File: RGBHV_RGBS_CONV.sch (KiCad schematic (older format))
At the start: 38 parts, among them J1 DIGITAL RGB, J10 AUDIO1, J11 RGBHV_2, J12 AUDIO2, J15 RGBS_OUT1, J16 RGBS_OUT2, J17 VIN, J2 VGA DB15, J3 ANALOG RGB DA15, J4 X1, J5 DIGITAL_RGBHV_1, J6 ANALOG RGB, J7 DIGITAL_RGBHV_2, J8 SWITCHER, J9 RGBHV_1, U1 OUT_GND_IN_3.3V, U2 74HC86, U3 OUT_IN_GND_3.3V

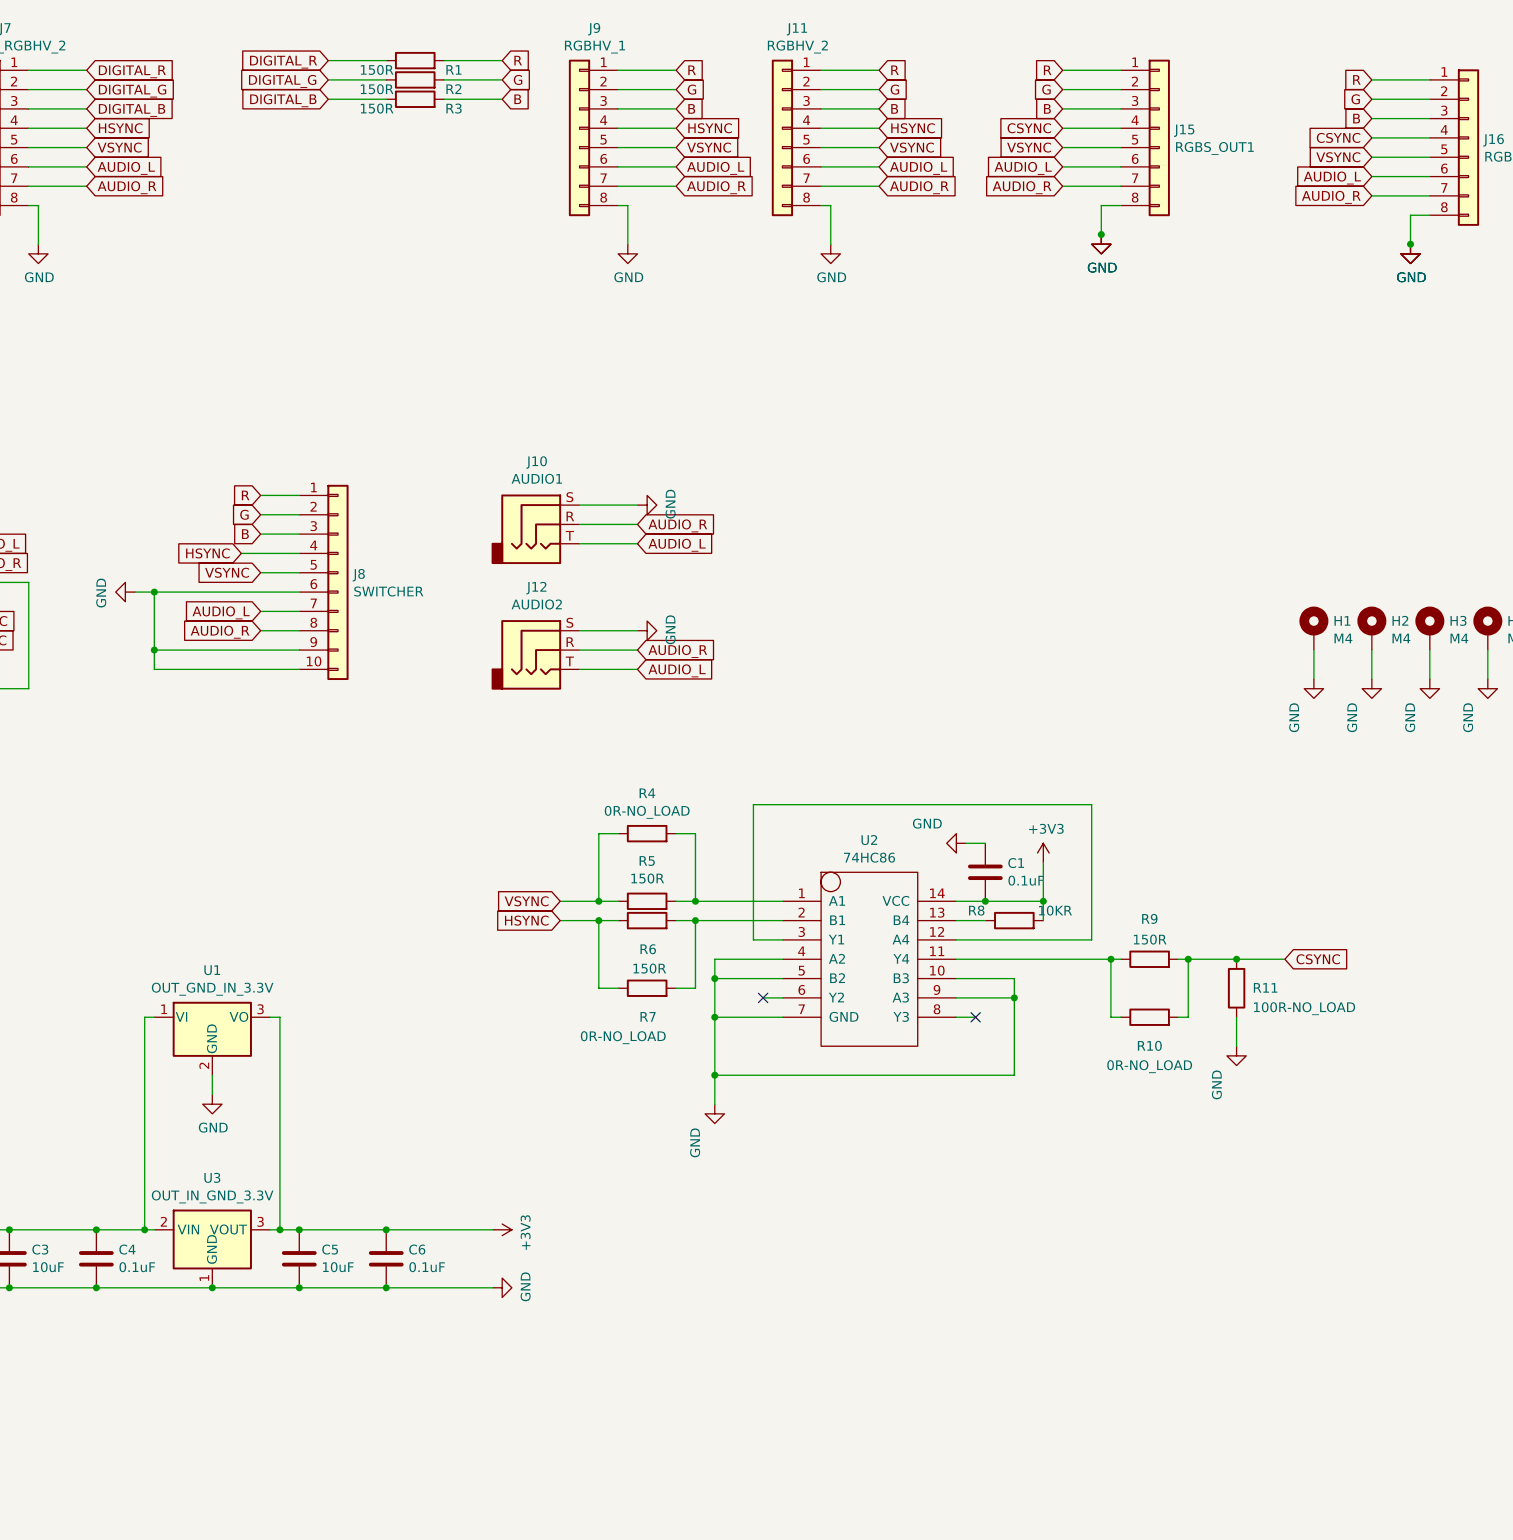
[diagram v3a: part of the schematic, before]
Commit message: Rev1.0C
レギュレータのパターンを追加。
RGBS XHコネクタへの音声パターンカット
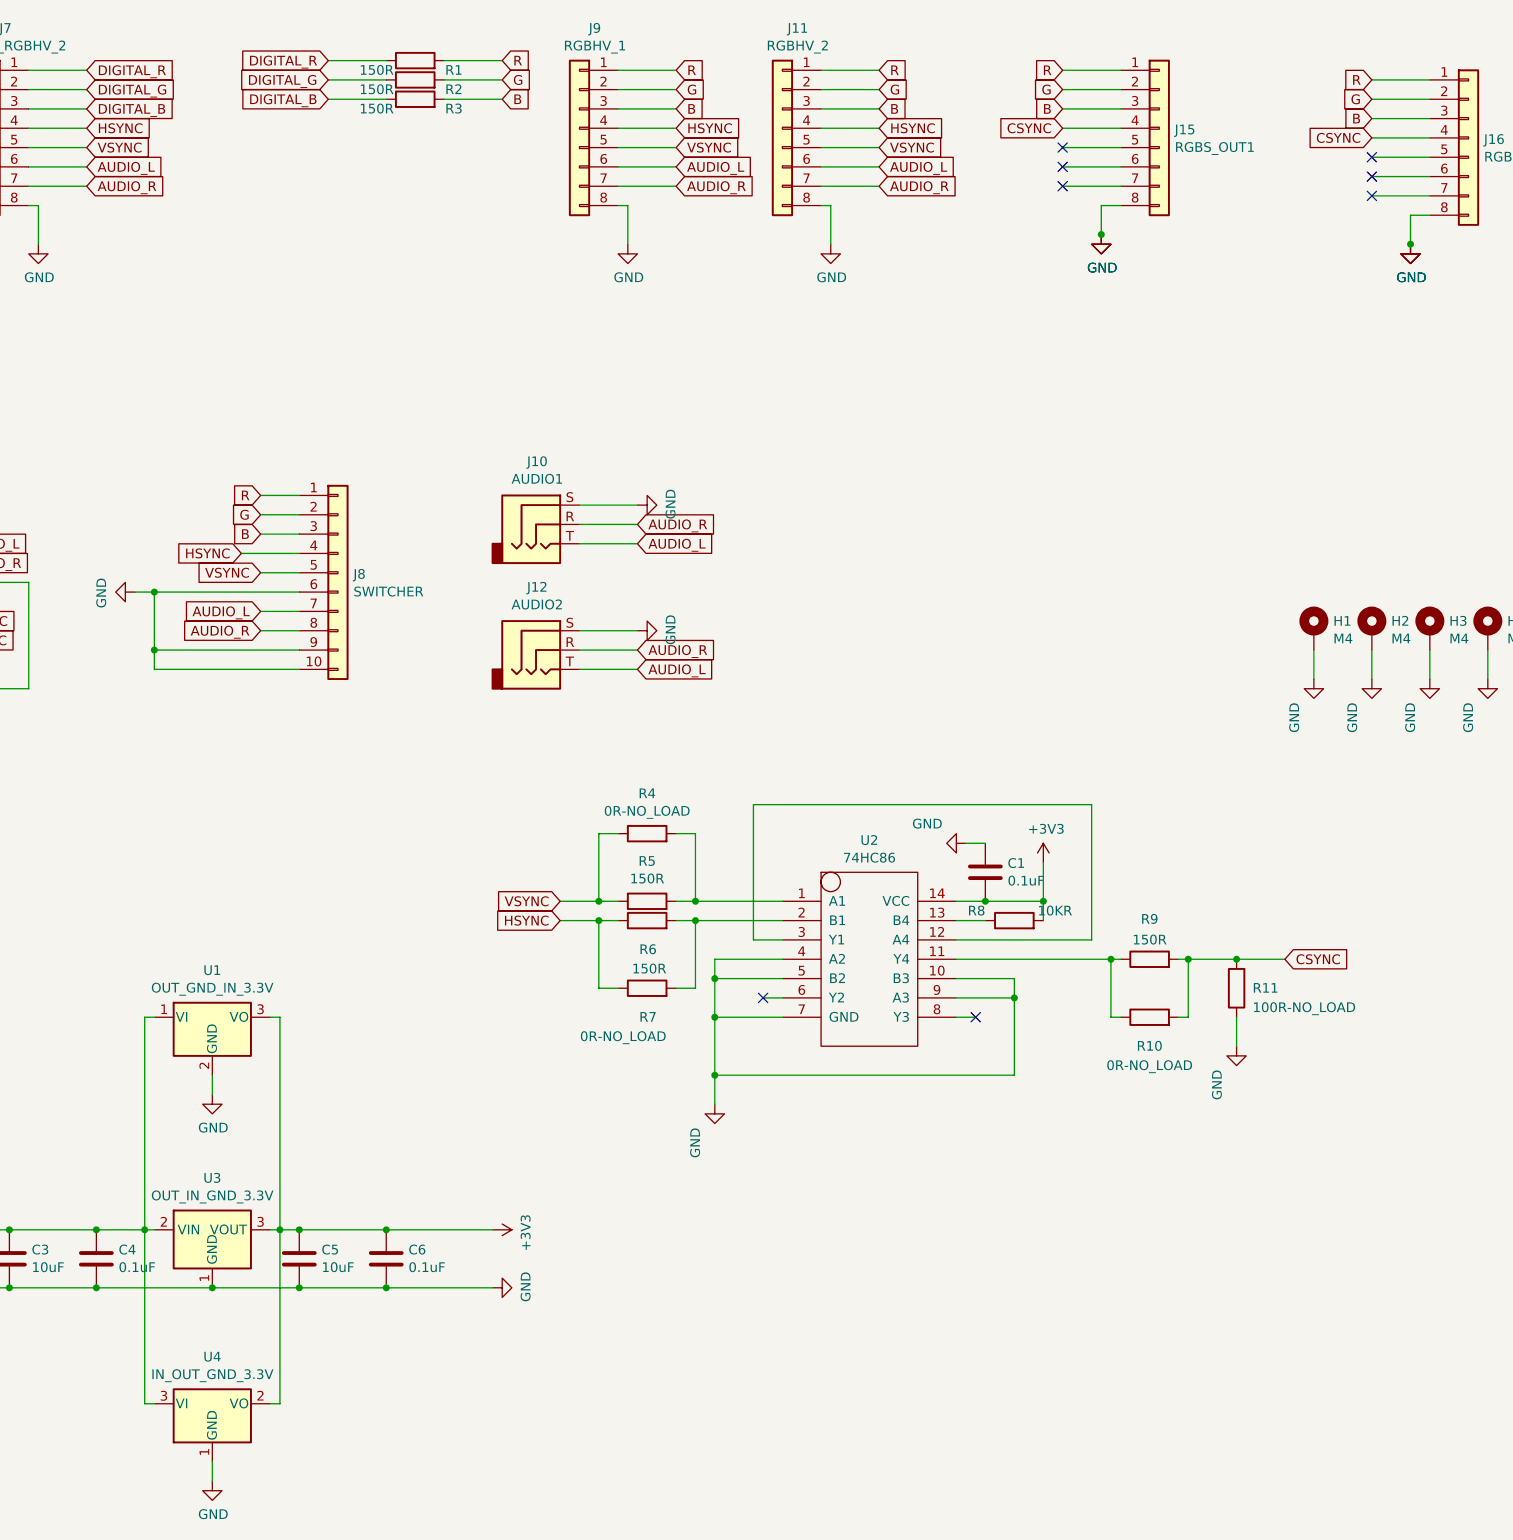
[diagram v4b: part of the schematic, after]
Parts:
- added U4: IN_OUT_GND_3.3V, Package_TO_SOT_THT:TO-220-3_Vertical, symbol Regulator_Linear:LM1117-3.3
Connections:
- net +3V3: now also U4.2 (VO)
- net AUDIO_L: no longer J15.6 (Pin_6), J16.6 (Pin_6)
- net AUDIO_R: no longer J15.7 (Pin_7), J16.7 (Pin_7)
- net GND: now also U4.1 (GND)
- net VSYNC: no longer J15.5 (Pin_5), J16.5 (Pin_5)
- net at C3.1, C4.1, J17.2 (Pin_2)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: now also U4.3 (VI)
- no-connect marks 16 -> 22
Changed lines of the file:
@@
 Wire Wire Line
 	12350 2150 12050 2150
-Text GLabel 12050 2150 0    50   Input ~ 0
-VSYNC
-Text GLabel 12050 2250 0    50   Input ~ 0
-AUDIO_L
-Text GLabel 12050 2350 0    50   Input ~ 0
-AUDIO_R
 Wire Wire Line
 	12050 2250 12350 2250
@@
 Wire Wire Line
 	13950 2200 13650 2200
-Text GLabel 13650 2200 0    50   Input ~ 0
-VSYNC
-Text GLabel 13650 2300 0    50   Input ~ 0
-AUDIO_L
-Text GLabel 13650 2400 0    50   Input ~ 0
-AUDIO_R
 Wire Wire Line
 	13650 2300 13950 2300
@@
 	0    1    1    0
 $EndComp
+$Comp
+L Regulator_Linear:LM1117-3.3 U4
+U 1 1 60C724BE
+P 7650 8650
+F 0 "U4" H 7650 8892 50  0000 C CNN
+F 1 "IN_OUT_GND_3.3V" H 7650 8801 50  0000 C CNN
+F 2 "Package_TO_SOT_THT:TO-220-3_Vertical" H 7650 8650 50  0001 C CNN
+F 3 "http://www.ti.com/lit/ds/symlink/lm1117.pdf" H 7650 8650 50  0001 C CNN
+	1    7650 8650
+	1    0    0    -1
+$EndComp
+Wire Wire Line
+	7300 7750 7300 8650
+Wire Wire Line
+	8000 7750 8000 8650
+Wire Wire Line
+	8000 8650 7950 8650
+Wire Wire Line
+	7350 8650 7300 8650
+$Comp
+L power:GND #PWR0108
+U 1 1 60CD679E
+P 7650 9050
+F 0 "#PWR0108" H 7650 8800 50  0001 C CNN
+F 1 "GND" H 7655 8877 50  0000 C CNN
+F 2 "" H 7650 9050 50  0001 C CNN
+F 3 "" H 7650 9050 50  0001 C CNN
+	1    7650 9050
+	1    0    0    -1
+$EndComp
+Wire Wire Line
+	7650 8950 7650 9050
+NoConn ~ 12050 2150
+NoConn ~ 12050 2250
+NoConn ~ 12050 2350
+NoConn ~ 13650 2200
+NoConn ~ 13650 2300
+NoConn ~ 13650 2400
 $EndSCHEMATC

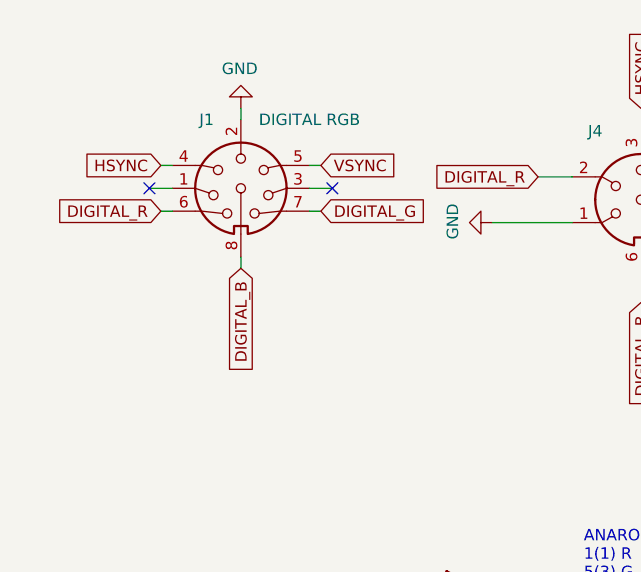
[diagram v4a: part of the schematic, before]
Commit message: Rev 1.0D
Fix DIN8 R-G H-V pin swap bug
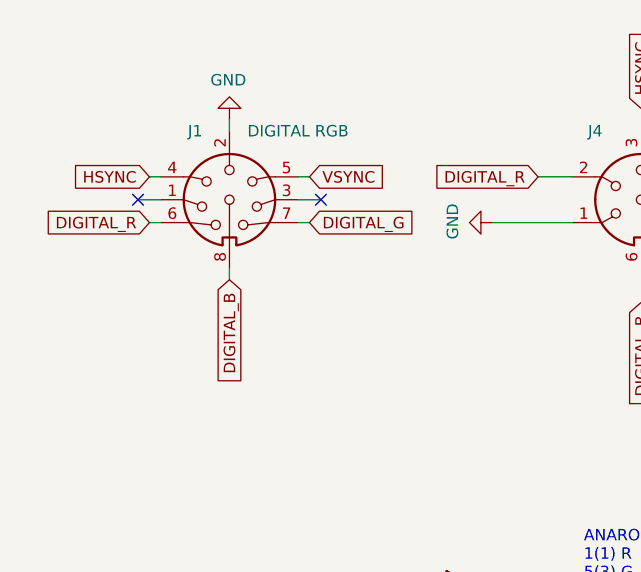
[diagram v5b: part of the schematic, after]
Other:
- moved on the sheet: J1
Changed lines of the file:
@@
 L Connector:DIN-8 J1
 U 1 1 5C43E8B2
-P 2200 2050
-F 0 "J1" H 2050 2350 50  0000 C CNN
-F 1 "DIGITAL RGB" H 2500 2350 50  0000 C CNN
-F 2 "ryuk_lib:DIN 8 PCB" H 2200 2050 50  0001 C CNN
-F 3 "http://www.mouser.com/ds/2/18/40_c091_abd_e-75918.pdf" H 2200 2050 50  0001 C CNN
-	1    2200 2050
+P 2150 2100
+F 0 "J1" H 2000 2400 50  0000 C CNN
+F 1 "DIGITAL RGB" H 2450 2400 50  0000 C CNN
+F 2 "ryuk_lib:DIN 8 PCB" H 2150 2100 50  0001 C CNN
+F 3 "http://www.mouser.com/ds/2/18/40_c091_abd_e-75918.pdf" H 2150 2100 50  0001 C CNN
+	1    2150 2100
 	1    0    0    -1
 $EndComp
@@
 $EndComp
 Wire Wire Line
-	1850 2150 1900 2150
-Wire Wire Line
-	2500 2150 2550 2150
-Wire Wire Line
-	2200 2350 2200 2400
-Wire Wire Line
-	1900 1950 1850 1950
-Wire Wire Line
-	2500 1950 2550 1950
-NoConn ~ 1800 2050
-NoConn ~ 2600 2050
+	1800 2200 1850 2200
+Wire Wire Line
+	2450 2200 2500 2200
+Wire Wire Line
+	2150 2400 2150 2450
+Wire Wire Line
+	1850 2000 1800 2000
+Wire Wire Line
+	2450 2000 2500 2000
+NoConn ~ 1750 2100
+NoConn ~ 2550 2100
 Wire Wire Line
 	12050 1750 12350 1750
@@
 Wire Wire Line
 	12050 2050 12350 2050
-Text GLabel 2550 2150 2    50   Input ~ 0
+Text GLabel 2500 2200 2    50   Input ~ 0
 DIGITAL_G
-Text GLabel 1850 2150 0    50   Input ~ 0
+Text GLabel 1800 2200 0    50   Input ~ 0
 DIGITAL_R
-Text GLabel 2200 2400 3    50   Input ~ 0
+Text GLabel 2150 2450 3    50   Input ~ 0
 DIGITAL_B
-Text GLabel 1850 1950 0    50   Input ~ 0
+Text GLabel 1800 2000 0    50   Input ~ 0
 HSYNC
-Text GLabel 2550 1950 2    50   Input ~ 0
+Text GLabel 2500 2000 2    50   Input ~ 0
 VSYNC
 Text GLabel 3500 2000 0    50   Input ~ 0
@@
 L power:GND #PWR01
 U 1 1 5CC0401E
-P 2200 1700
-F 0 "#PWR01" H 2200 1450 50  0001 C CNN
-F 1 "GND" H 2205 1527 50  0000 C CNN
-F 2 "" H 2200 1700 50  0001 C CNN
-F 3 "" H 2200 1700 50  0001 C CNN
-	1    2200 1700
+P 2150 1750
+F 0 "#PWR01" H 2150 1500 50  0001 C CNN
+F 1 "GND" H 2155 1577 50  0000 C CNN
+F 2 "" H 2150 1750 50  0001 C CNN
+F 3 "" H 2150 1750 50  0001 C CNN
+	1    2150 1750
 	-1   0    0    1
 $EndComp
 Wire Wire Line
-	2200 1700 2200 1750
+	2150 1750 2150 1800
 $Comp
 L power:GND #PWR06
@@
 	12700 6350 12950 6350
 Wire Wire Line
-	2500 2050 2600 2050
-Wire Wire Line
-	1800 2050 1900 2050
+	2450 2100 2550 2100
+Wire Wire Line
+	1750 2100 1850 2100
 Text GLabel 5700 2250 2    50   Input ~ 0
 AUDIO_L
